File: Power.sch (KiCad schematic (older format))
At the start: 16 parts

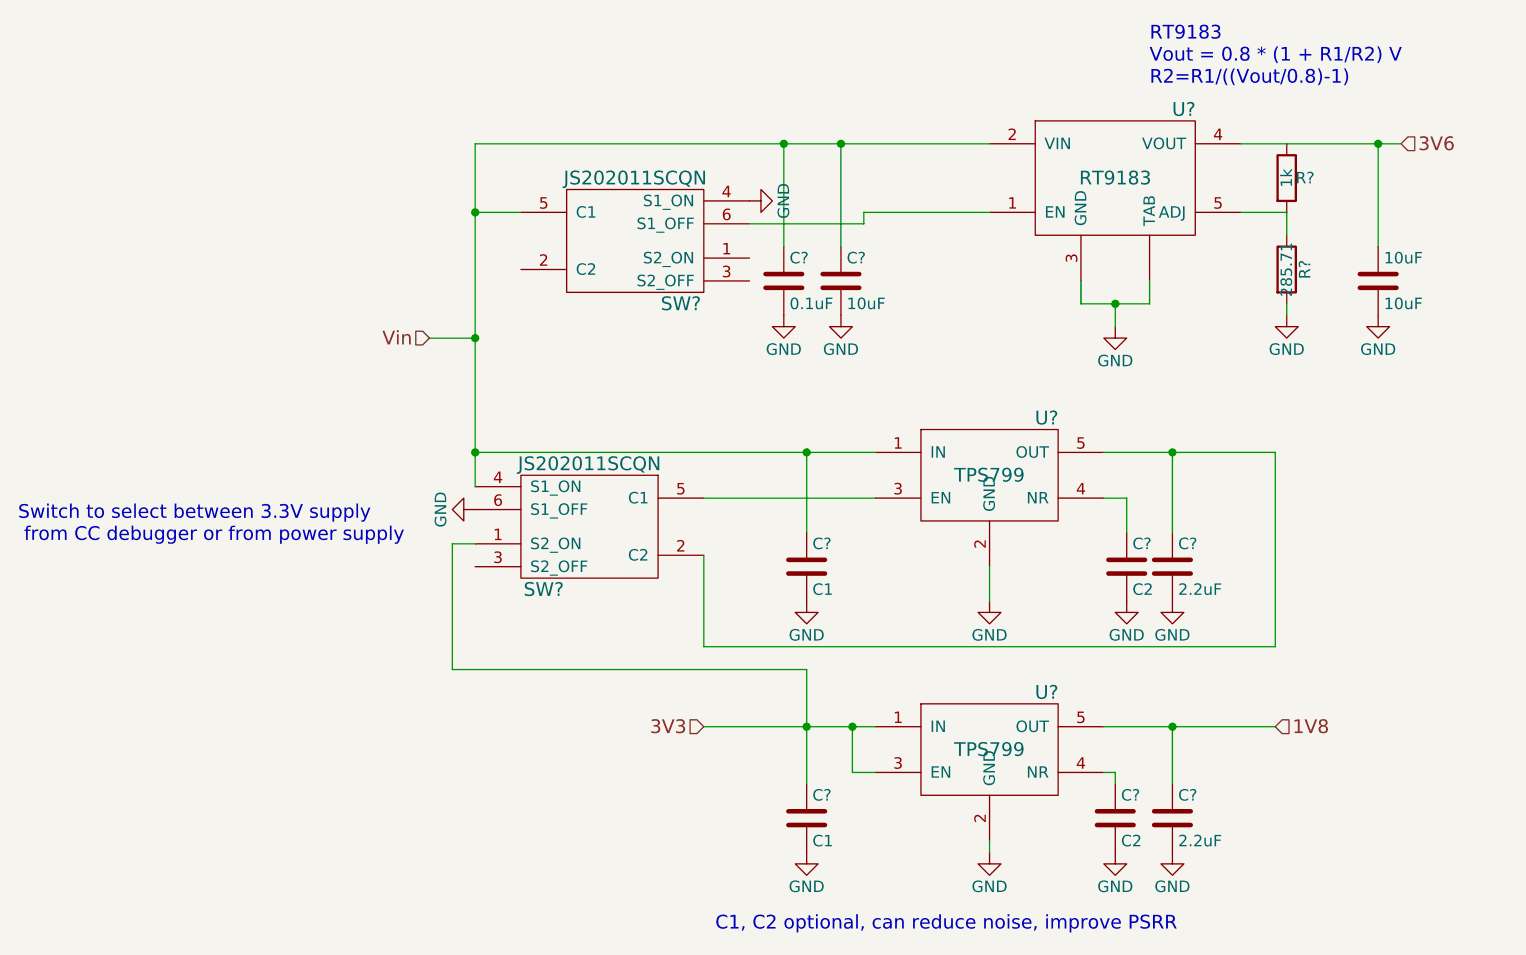
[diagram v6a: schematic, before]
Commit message: added a bunch of footprints and generated layout file
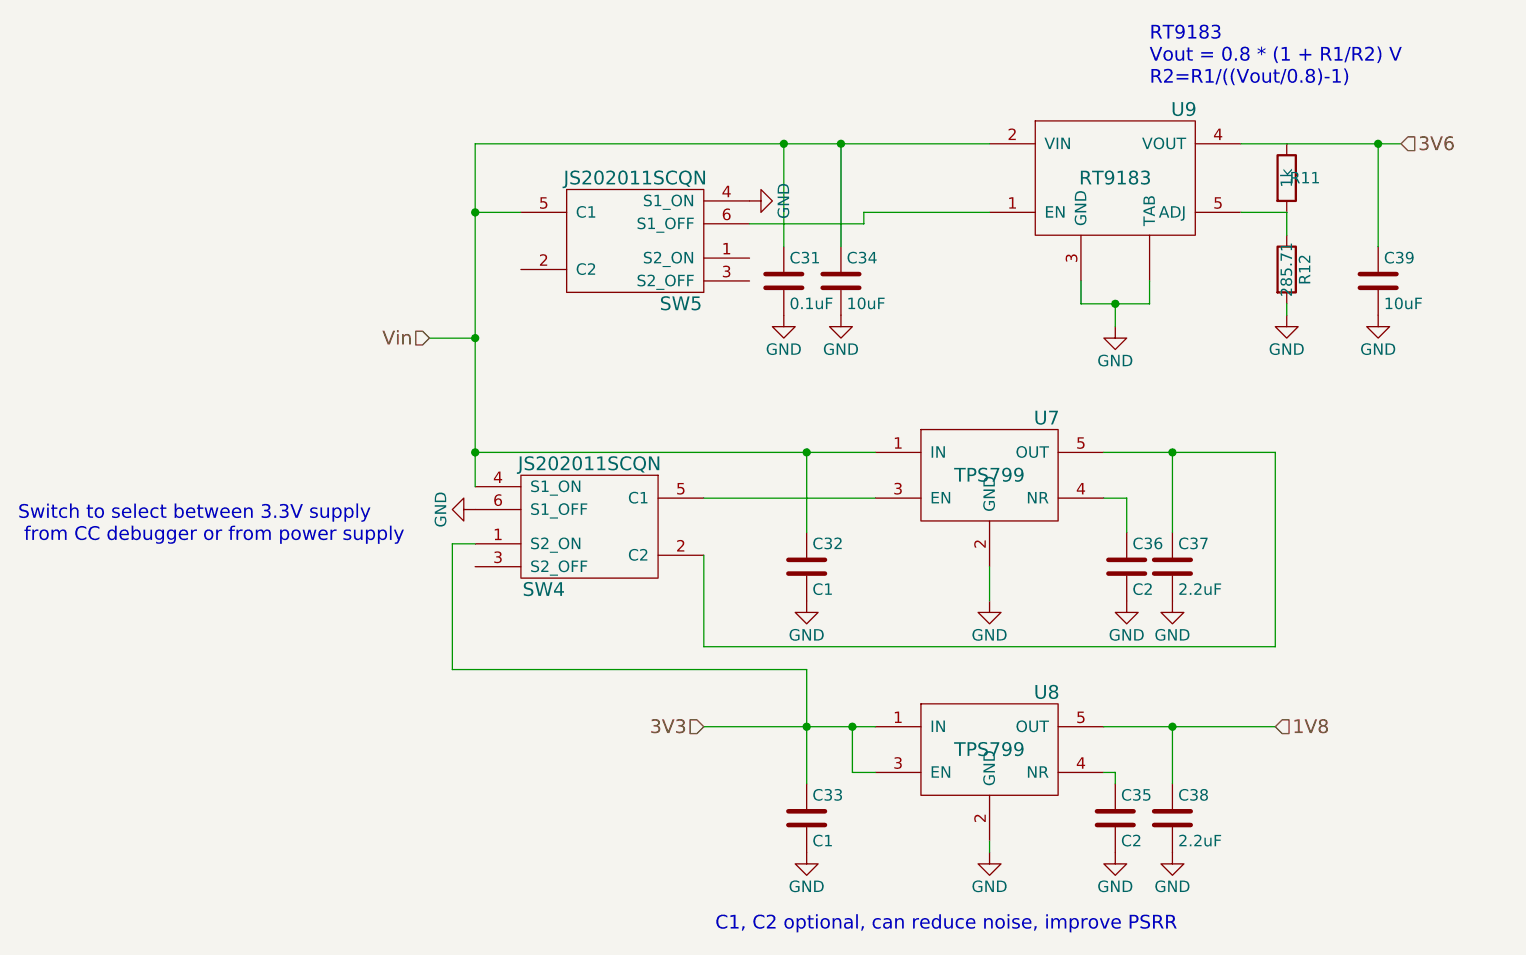
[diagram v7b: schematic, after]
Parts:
- C31, C32, C33, C34, C35, C36, C37, C38: renamed from C?; footprint (none) -> Capacitors_SMD:C_0402
- C39: renamed from 10uF; footprint (none) -> Capacitors_SMD:C_0402
- R11, R12: renamed from R?; footprint (none) -> Resistors_SMD:R_0402
- SW4, SW5: renamed from SW?; footprint (none) -> SFUSat-Radio:JS2020_SMD
- U7, U8: renamed from U?; footprint (none) -> SFUSat-Radio:PDSO-G5
- U9: renamed from U?; footprint (none) -> TO_SOT_Packages_SMD:TO-263-5Lead
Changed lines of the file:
@@
 1V8
 $Comp
-L RT9183 U?
+L RT9183 U9
 U 1 1 58770580
 P 6900 2150
-F 0 "U?" H 7200 2450 60  0000 C CNN
+F 0 "U9" H 7200 2450 60  0000 C CNN
 F 1 "RT9183" H 6900 2150 60  0000 C CNN
-F 2 "" H 6900 2150 60  0001 C CNN
+F 2 "TO_SOT_Packages_SMD:TO-263-5Lead" H 6900 2150 60  0001 C CNN
 F 3 "" H 6900 2150 60  0001 C CNN
 	1    6900 2150
@@
 $EndComp
 $Comp
-L C C?
+L C C34
 U 1 1 587706B0
 P 5700 2600
-F 0 "C?" H 5725 2700 50  0000 L CNN
+F 0 "C34" H 5725 2700 50  0000 L CNN
 F 1 "10uF" H 5725 2500 50  0000 L CNN
-F 2 "" H 5738 2450 50  0000 C CNN
+F 2 "Capacitors_SMD:C_0402" H 5738 2450 50  0001 C CNN
 F 3 "" H 5700 2600 50  0000 C CNN
 	1    5700 2600
@@
 $EndComp
 $Comp
-L C C?
+L C C31
 U 1 1 58770789
 P 5450 2600
-F 0 "C?" H 5475 2700 50  0000 L CNN
+F 0 "C31" H 5475 2700 50  0000 L CNN
 F 1 "0.1uF" H 5475 2500 50  0000 L CNN
-F 2 "" H 5488 2450 50  0000 C CNN
+F 2 "Capacitors_SMD:C_0402" H 5488 2450 50  0001 C CNN
 F 3 "" H 5450 2600 50  0000 C CNN
 	1    5450 2600
@@
 $EndComp
 $Comp
-L GND #PWR?
+L GND #PWR041
 U 1 1 58770941
 P 6900 2800
-F 0 "#PWR?" H 6900 2550 50  0001 C CNN
+F 0 "#PWR041" H 6900 2550 50  0001 C CNN
 F 1 "GND" H 6900 2650 50  0000 C CNN
 F 2 "" H 6900 2800 50  0000 C CNN
@@
 $EndComp
 $Comp
-L C 10uF
+L C C39
 U 1 1 58770AC4
 P 8050 2600
-F 0 "10uF" H 8075 2700 50  0000 L CNN
+F 0 "C39" H 8075 2700 50  0000 L CNN
 F 1 "10uF" H 8075 2500 50  0000 L CNN
-F 2 "" H 8088 2450 50  0000 C CNN
+F 2 "Capacitors_SMD:C_0402" H 8088 2450 50  0001 C CNN
 F 3 "" H 8050 2600 50  0000 C CNN
 	1    8050 2600
@@
 $EndComp
 $Comp
-L GND #PWR?
+L GND #PWR042
 U 1 1 58770B93
 P 8050 2750
-F 0 "#PWR?" H 8050 2500 50  0001 C CNN
+F 0 "#PWR042" H 8050 2500 50  0001 C CNN
 F 1 "GND" H 8050 2600 50  0000 C CNN
 F 2 "" H 8050 2750 50  0000 C CNN
@@
 $EndComp
 $Comp
-L GND #PWR?
+L GND #PWR043
 U 1 1 58770BD7
 P 7650 2750
-F 0 "#PWR?" H 7650 2500 50  0001 C CNN
+F 0 "#PWR043" H 7650 2500 50  0001 C CNN
 F 1 "GND" H 7650 2600 50  0000 C CNN
 F 2 "" H 7650 2750 50  0000 C CNN
@@
 $EndComp
 $Comp
-L GND #PWR?
+L GND #PWR044
 U 1 1 58770CCB
 P 5700 2750
-F 0 "#PWR?" H 5700 2500 50  0001 C CNN
+F 0 "#PWR044" H 5700 2500 50  0001 C CNN
 F 1 "GND" H 5700 2600 50  0000 C CNN
 F 2 "" H 5700 2750 50  0000 C CNN
@@
 $EndComp
 $Comp
-L GND #PWR?
+L GND #PWR045
 U 1 1 58770CE7
 P 5450 2750
-F 0 "#PWR?" H 5450 2500 50  0001 C CNN
+F 0 "#PWR045" H 5450 2500 50  0001 C CNN
 F 1 "GND" H 5450 2600 50  0000 C CNN
 F 2 "" H 5450 2750 50  0000 C CNN
@@
 $EndComp
 $Comp
-L R R?
+L R R12
 U 1 1 58770EF4
 P 7650 2550
-F 0 "R?" V 7730 2550 50  0000 C CNN
+F 0 "R12" V 7730 2550 50  0000 C CNN
 F 1 "285.71" V 7650 2550 50  0000 C CNN
-F 2 "" V 7580 2550 50  0000 C CNN
+F 2 "Resistors_SMD:R_0402" V 7580 2550 50  0001 C CNN
 F 3 "" H 7650 2550 50  0000 C CNN
 	1    7650 2550
@@
 $EndComp
 $Comp
-L R R?
+L R R11
 U 1 1 58770EC5
 P 7650 2150
-F 0 "R?" H 7730 2150 50  0000 C CNN
+F 0 "R11" H 7730 2150 50  0000 C CNN
 F 1 "1k" V 7650 2150 50  0000 C CNN
-F 2 "" V 7580 2150 50  0000 C CNN
+F 2 "Resistors_SMD:R_0402" V 7580 2150 50  0001 C CNN
 F 3 "" H 7650 2150 50  0000 C CNN
 	1    7650 2150
@@
 RT9183\nVout = 0.8 * (1 + R1/R2) V\nR2=R1/((Vout/0.8)-1)
 $Comp
-L TPS799 U?
+L TPS799 U7
 U 1 1 5879CF29
 P 6350 3450
-F 0 "U?" H 6600 3700 60  0000 C CNN
+F 0 "U7" H 6600 3700 60  0000 C CNN
 F 1 "TPS799" H 6350 3450 60  0000 C CNN
-F 2 "" H 6350 3450 60  0001 C CNN
+F 2 "SFUSat-Radio:PDSO-G5" H 6350 3450 60  0001 C CNN
 F 3 "" H 6350 3450 60  0001 C CNN
 	1    6350 3450
@@
 $EndComp
 $Comp
-L GND #PWR?
+L GND #PWR046
 U 1 1 5879D9E2
 P 6350 4000
-F 0 "#PWR?" H 6350 3750 50  0001 C CNN
+F 0 "#PWR046" H 6350 3750 50  0001 C CNN
 F 1 "GND" H 6350 3850 50  0000 C CNN
 F 2 "" H 6350 4000 50  0000 C CNN
@@
 $EndComp
 $Comp
-L GND #PWR?
+L GND #PWR047
 U 1 1 5879DA04
 P 7150 4000
-F 0 "#PWR?" H 7150 3750 50  0001 C CNN
+F 0 "#PWR047" H 7150 3750 50  0001 C CNN
 F 1 "GND" H 7150 3850 50  0000 C CNN
 F 2 "" H 7150 4000 50  0000 C CNN
@@
 $EndComp
 $Comp
-L GND #PWR?
+L GND #PWR048
 U 1 1 5879DA26
 P 6950 4000
-F 0 "#PWR?" H 6950 3750 50  0001 C CNN
+F 0 "#PWR048" H 6950 3750 50  0001 C CNN
 F 1 "GND" H 6950 3850 50  0000 C CNN
 F 2 "" H 6950 4000 50  0000 C CNN
@@
 $EndComp
 $Comp
-L C C?
+L C C36
 U 1 1 5879DA48
 P 6950 3850
-F 0 "C?" H 6975 3950 50  0000 L CNN
+F 0 "C36" H 6975 3950 50  0000 L CNN
 F 1 "C2" H 6975 3750 50  0000 L CNN
-F 2 "" H 6988 3700 50  0000 C CNN
+F 2 "Capacitors_SMD:C_0402" H 6988 3700 50  0001 C CNN
 F 3 "" H 6950 3850 50  0000 C CNN
 	1    6950 3850
@@
 $EndComp
 $Comp
-L C C?
+L C C37
 U 1 1 5879DAAB
 P 7150 3850
-F 0 "C?" H 7175 3950 50  0000 L CNN
+F 0 "C37" H 7175 3950 50  0000 L CNN
 F 1 "2.2uF" H 7175 3750 50  0000 L CNN
-F 2 "" H 7188 3700 50  0000 C CNN
+F 2 "Capacitors_SMD:C_0402" H 7188 3700 50  0001 C CNN
 F 3 "" H 7150 3850 50  0000 C CNN
 	1    7150 3850
@@
 $EndComp
 $Comp
-L GND #PWR?
+L GND #PWR049
 U 1 1 5879E264
 P 5550 4000
-F 0 "#PWR?" H 5550 3750 50  0001 C CNN
+F 0 "#PWR049" H 5550 3750 50  0001 C CNN
 F 1 "GND" H 5550 3850 50  0000 C CNN
 F 2 "" H 5550 4000 50  0000 C CNN
@@
 $EndComp
 $Comp
-L C C?
+L C C32
 U 1 1 5879E323
 P 5550 3850
-F 0 "C?" H 5575 3950 50  0000 L CNN
+F 0 "C32" H 5575 3950 50  0000 L CNN
 F 1 "C1" H 5575 3750 50  0000 L CNN
-F 2 "" H 5588 3700 50  0000 C CNN
+F 2 "Capacitors_SMD:C_0402" H 5588 3700 50  0001 C CNN
 F 3 "" H 5550 3850 50  0000 C CNN
 	1    5550 3850
@@
 $EndComp
 $Comp
-L TPS799 U?
+L TPS799 U8
 U 1 1 587A1254
 P 6350 4650
-F 0 "U?" H 6600 4900 60  0000 C CNN
+F 0 "U8" H 6600 4900 60  0000 C CNN
 F 1 "TPS799" H 6350 4650 60  0000 C CNN
-F 2 "" H 6350 4650 60  0001 C CNN
+F 2 "SFUSat-Radio:PDSO-G5" H 6350 4650 60  0001 C CNN
 F 3 "" H 6350 4650 60  0001 C CNN
 	1    6350 4650
@@
 $EndComp
 $Comp
-L C C?
+L C C33
 U 1 1 587A1577
 P 5550 4950
-F 0 "C?" H 5575 5050 50  0000 L CNN
+F 0 "C33" H 5575 5050 50  0000 L CNN
 F 1 "C1" H 5575 4850 50  0000 L CNN
-F 2 "" H 5588 4800 50  0000 C CNN
+F 2 "Capacitors_SMD:C_0402" H 5588 4800 50  0001 C CNN
 F 3 "" H 5550 4950 50  0000 C CNN
 	1    5550 4950
@@
 $EndComp
 $Comp
-L GND #PWR?
+L GND #PWR050
 U 1 1 587A177D
 P 5550 5100
-F 0 "#PWR?" H 5550 4850 50  0001 C CNN
+F 0 "#PWR050" H 5550 4850 50  0001 C CNN
 F 1 "GND" H 5550 4950 50  0000 C CNN
 F 2 "" H 5550 5100 50  0000 C CNN
@@
 $EndComp
 $Comp
-L C C?
+L C C35
 U 1 1 587A1EB3
 P 6900 4950
-F 0 "C?" H 6925 5050 50  0000 L CNN
+F 0 "C35" H 6925 5050 50  0000 L CNN
 F 1 "C2" H 6925 4850 50  0000 L CNN
-F 2 "" H 6938 4800 50  0000 C CNN
+F 2 "Capacitors_SMD:C_0402" H 6938 4800 50  0001 C CNN
 F 3 "" H 6900 4950 50  0000 C CNN
 	1    6900 4950
@@
 $EndComp
 $Comp
-L GND #PWR?
+L GND #PWR051
 U 1 1 587A201C
 P 6900 5100
-F 0 "#PWR?" H 6900 4850 50  0001 C CNN
+F 0 "#PWR051" H 6900 4850 50  0001 C CNN
 F 1 "GND" H 6900 4950 50  0000 C CNN
 F 2 "" H 6900 5100 50  0000 C CNN
@@
 $EndComp
 $Comp
-L C C?
+L C C38
 U 1 1 587A204E
 P 7150 4950
-F 0 "C?" H 7175 5050 50  0000 L CNN
+F 0 "C38" H 7175 5050 50  0000 L CNN
 F 1 "2.2uF" H 7175 4850 50  0000 L CNN
-F 2 "" H 7188 4800 50  0000 C CNN
+F 2 "Capacitors_SMD:C_0402" H 7188 4800 50  0001 C CNN
 F 3 "" H 7150 4950 50  0000 C CNN
 	1    7150 4950
@@
 $EndComp
 $Comp
-L GND #PWR?
+L GND #PWR052
 U 1 1 587A209C
 P 7150 5100
-F 0 "#PWR?" H 7150 4850 50  0001 C CNN
+F 0 "#PWR052" H 7150 4850 50  0001 C CNN
 F 1 "GND" H 7150 4950 50  0000 C CNN
 F 2 "" H 7150 5100 50  0000 C CNN
@@
 $EndComp
 $Comp
-L GND #PWR?
+L GND #PWR053
 U 1 1 587A2F8C
 P 6350 5100
-F 0 "#PWR?" H 6350 4850 50  0001 C CNN
+F 0 "#PWR053" H 6350 4850 50  0001 C CNN
 F 1 "GND" H 6350 4950 50  0000 C CNN
 F 2 "" H 6350 5100 50  0000 C CNN
@@
 C1, C2 optional, can reduce noise, improve PSRR
 $Comp
-L JS202011SCQN SW?
+L JS202011SCQN SW5
 U 1 1 587D58F9
 P 4800 2300
-F 0 "SW?" H 5000 1900 60  0000 C CNN
+F 0 "SW5" H 5000 1900 60  0000 C CNN
 F 1 "JS202011SCQN" H 4800 2450 60  0000 C CNN
-F 2 "" H 4800 2300 60  0000 C CNN
+F 2 "SFUSat-Radio:JS2020_SMD" H 4800 2300 60  0001 C CNN
 F 3 "" H 4800 2300 60  0000 C CNN
 	1    4800 2300
@@
 $EndComp
 $Comp
-L JS202011SCQN SW?
+L JS202011SCQN SW4
 U 1 1 587D6D34
 P 4600 3550
-F 0 "SW?" H 4800 3150 60  0000 C CNN
+F 0 "SW4" H 4800 3150 60  0000 C CNN
 F 1 "JS202011SCQN" H 4600 3700 60  0000 C CNN
-F 2 "" H 4600 3550 60  0000 C CNN
+F 2 "SFUSat-Radio:JS2020_SMD" H 4600 3550 60  0001 C CNN
 F 3 "" H 4600 3550 60  0000 C CNN
 	1    4600 3550
@@
 $EndComp
 $Comp
-L GND #PWR?
+L GND #PWR054
 U 1 1 587D7AEC
 P 5300 2250
-F 0 "#PWR?" H 5300 2000 50  0001 C CNN
+F 0 "#PWR054" H 5300 2000 50  0001 C CNN
 F 1 "GND" H 5300 2100 50  0000 C CNN
 F 2 "" H 5300 2250 50  0000 C CNN
@@
 $EndComp
 $Comp
-L GND #PWR?
+L GND #PWR055
 U 1 1 587D7DE0
 P 4100 3600
-F 0 "#PWR?" H 4100 3350 50  0001 C CNN
+F 0 "#PWR055" H 4100 3350 50  0001 C CNN
 F 1 "GND" H 4100 3450 50  0000 C CNN
 F 2 "" H 4100 3600 50  0000 C CNN

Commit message: deleted a useless switch
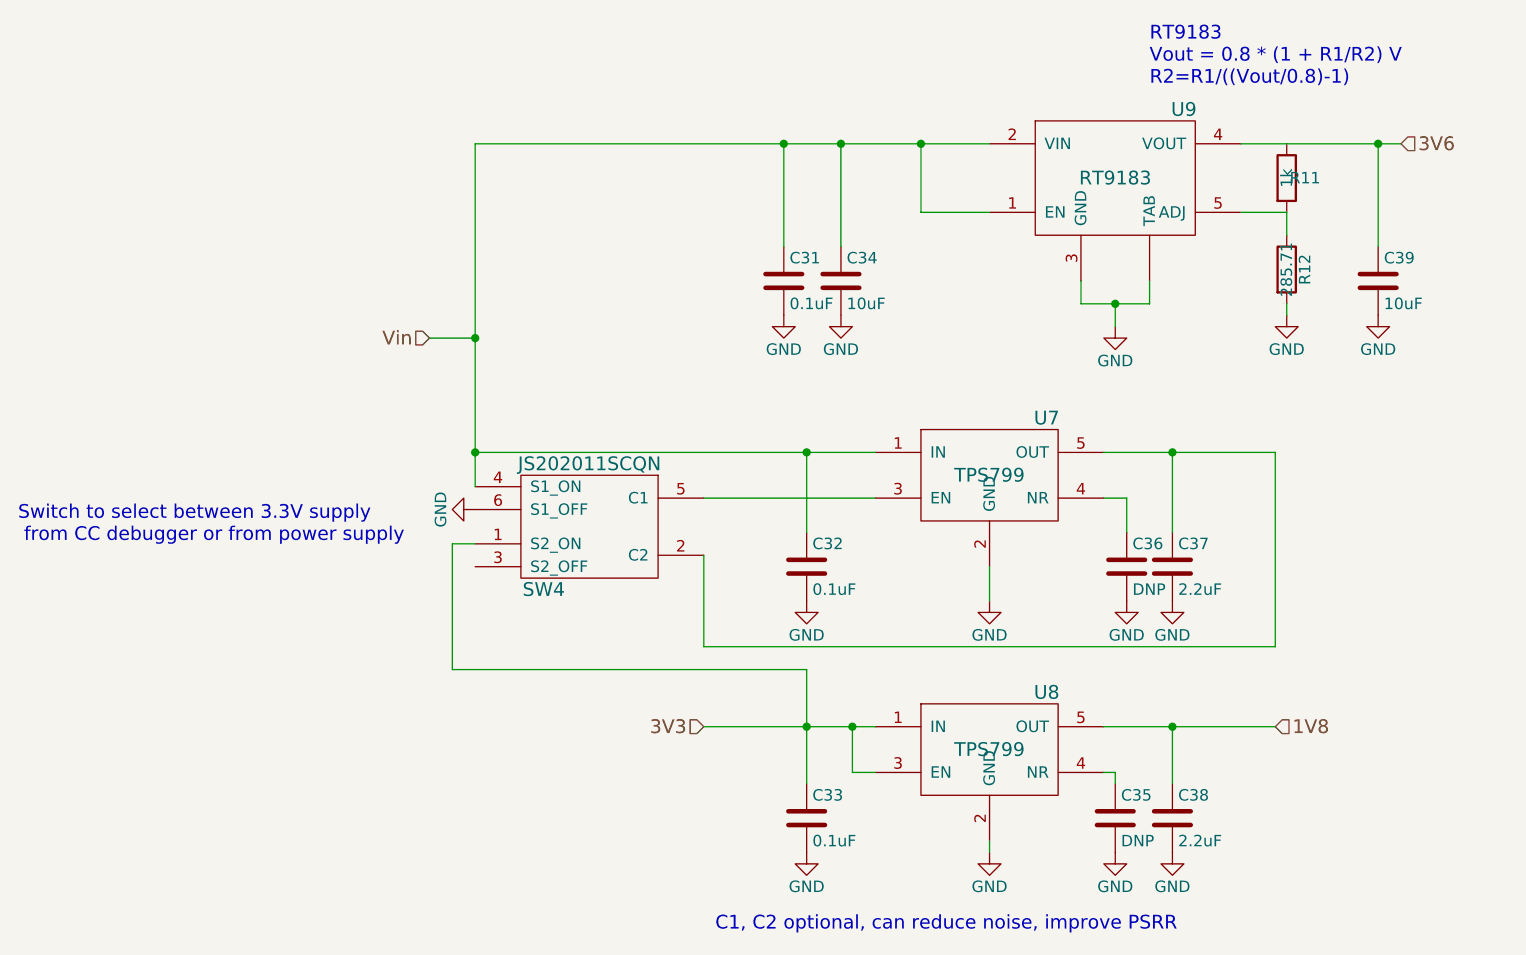
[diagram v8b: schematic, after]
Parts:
- removed SW5: JS202011SCQN, SFUSat-Radio:JS2020_SMD, symbol JS202011SCQN
- C32, C33: value C1 -> 0.1uF
- C35, C36: value C2 -> DNP
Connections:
- net Vin: now also U9.1 (EN)
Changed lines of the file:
@@
 P 6950 3850
 F 0 "C36" H 6975 3950 50  0000 L CNN
-F 1 "C2" H 6975 3750 50  0000 L CNN
+F 1 "DNP" H 6975 3750 50  0000 L CNN
 F 2 "Capacitors_SMD:C_0402" H 6988 3700 50  0001 C CNN
 F 3 "" H 6950 3850 50  0000 C CNN
@@
 P 5550 3850
 F 0 "C32" H 5575 3950 50  0000 L CNN
-F 1 "C1" H 5575 3750 50  0000 L CNN
+F 1 "0.1uF" H 5575 3750 50  0000 L CNN
 F 2 "Capacitors_SMD:C_0402" H 5588 3700 50  0001 C CNN
 F 3 "" H 5550 3850 50  0000 C CNN
@@
 P 5550 4950
 F 0 "C33" H 5575 5050 50  0000 L CNN
-F 1 "C1" H 5575 4850 50  0000 L CNN
+F 1 "0.1uF" H 5575 4850 50  0000 L CNN
 F 2 "Capacitors_SMD:C_0402" H 5588 4800 50  0001 C CNN
 F 3 "" H 5550 4950 50  0000 C CNN
@@
 P 6900 4950
 F 0 "C35" H 6925 5050 50  0000 L CNN
-F 1 "C2" H 6925 4850 50  0000 L CNN
+F 1 "DNP" H 6925 4850 50  0000 L CNN
 F 2 "Capacitors_SMD:C_0402" H 6938 4800 50  0001 C CNN
 F 3 "" H 6900 4950 50  0000 C CNN
@@
 Text Notes 5150 5450 0    60   ~ 0
 C1, C2 optional, can reduce noise, improve PSRR
-$Comp
-L JS202011SCQN SW5
-U 1 1 587D58F9
-P 4800 2300
-F 0 "SW5" H 5000 1900 60  0000 C CNN
-F 1 "JS202011SCQN" H 4800 2450 60  0000 C CNN
-F 2 "SFUSat-Radio:JS2020_SMD" H 4800 2300 60  0001 C CNN
-F 3 "" H 4800 2300 60  0000 C CNN
-	1    4800 2300
-	1    0    0    -1
-$EndComp
 $Comp
 L JS202011SCQN SW4
@@
 $EndComp
 $Comp
-L GND #PWR054
-U 1 1 587D7AEC
-P 5300 2250
-F 0 "#PWR054" H 5300 2000 50  0001 C CNN
-F 1 "GND" H 5300 2100 50  0000 C CNN
-F 2 "" H 5300 2250 50  0000 C CNN
-F 3 "" H 5300 2250 50  0000 C CNN
-	1    5300 2250
-	0    -1   -1   0
-$EndComp
-$Comp
 L GND #PWR055
 U 1 1 587D7DE0
@@
 	4100 3350 5850 3350
 Connection ~ 4100 3350
-Connection ~ 4100 2300
 Wire Wire Line
 	4100 2850 3900 2850
@@
 Connection ~ 5750 4550
 Wire Wire Line
-	4300 2300 4100 2300
-Wire Wire Line
 	5700 2450 5700 2000
 Wire Wire Line
@@
 Connection ~ 5450 2000
 Wire Wire Line
-	5300 2350 5800 2350
-Wire Wire Line
-	5800 2350 5800 2300
-Wire Wire Line
 	7600 3350 7600 4200
 Wire Wire Line
 	5550 4300 5550 4800
-Wire Wire Line
-	5800 2300 6350 2300
 Wire Wire Line
 	5100 4550 5850 4550
@@
 Wire Wire Line
 	4000 3750 4100 3750
+Wire Wire Line
+	6350 2300 6050 2300
+Wire Wire Line
+	6050 2300 6050 2000
+Connection ~ 6050 2000
 $EndSCHEMATC
